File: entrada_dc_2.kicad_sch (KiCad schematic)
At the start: 4 parts

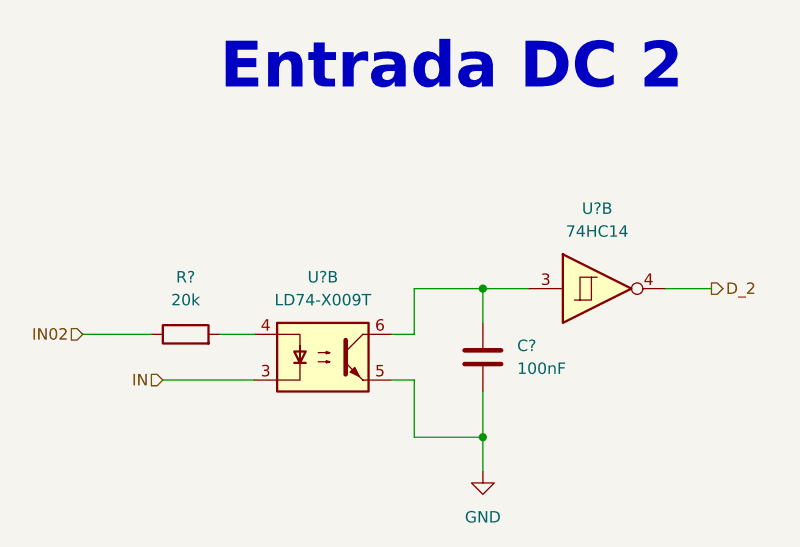
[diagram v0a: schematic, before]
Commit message: input/output separadas
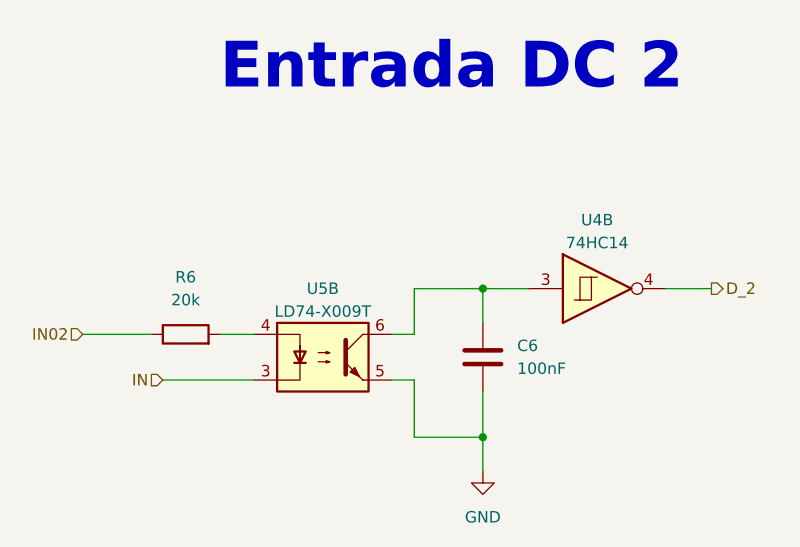
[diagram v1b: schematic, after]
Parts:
- gave numbers to parts that had none: 4
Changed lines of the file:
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@@
 (kicad_sch (version 20221004) (generator eeschema)
   (paper "A4" portrait)
+  (title_block
+    (date "2022-10-09")
+    (rev "José Luis Laica")
+  )
   (junction (at 113.03 138.43) (diameter 0) (color 0 0 0 0)
   )
@@
   (symbol (lib_id "power:GND") (at 113.03 142.24 0) (unit 1)
     (in_bom yes) (on_board yes) (dnp no) (fields_autoplaced)
-    (property "Reference" "#PWR?" (at 113.03 148.59 0)
+    (property "Reference" "#PWR07" (at 113.03 148.59 0)
       (effects (font (size 1.27 1.27)) hide)
     )
@@
       (project "PLC 32 V2"
         (path "/d17a54f1-6eda-453f-95e1-42a53b02a1c3/7b2fc48b-830b-4449-9557-444c529d204e"
-          (reference "#PWR?") (unit 1) (value "GND") (footprint "")
+          (reference "#PWR07") (unit 1) (value "GND") (footprint "")
         )
       )
@@
   (symbol (lib_id "Device:C") (at 113.03 129.54 0) (unit 1)
     (in_bom yes) (on_board yes) (dnp no) (fields_autoplaced)
-    (property "Reference" "C?" (at 116.84 128.2699 0)
+    (property "Reference" "C6" (at 116.84 128.2699 0)
       (effects (font (size 1.27 1.27)) (justify left))
     )
@@
       (project "PLC 32 V2"
         (path "/d17a54f1-6eda-453f-95e1-42a53b02a1c3/7b2fc48b-830b-4449-9557-444c529d204e"
-          (reference "C?") (unit 1) (value "100nF") (footprint "Capacitor_SMD:C_0402_1005Metric")
+          (reference "C6") (unit 1) (value "100nF") (footprint "Capacitor_SMD:C_0402_1005Metric")
         )
       )
@@
   (symbol (lib_id "Device:R") (at 80.01 127 90) (unit 1)
     (in_bom yes) (on_board yes) (dnp no) (fields_autoplaced)
-    (property "Reference" "R?" (at 80.01 120.65 90)
+    (property "Reference" "R6" (at 80.01 120.65 90)
       (effects (font (size 1.27 1.27)))
     )
@@
       (project "PLC 32 V2"
         (path "/d17a54f1-6eda-453f-95e1-42a53b02a1c3/7b2fc48b-830b-4449-9557-444c529d204e"
-          (reference "R?") (unit 1) (value "20k") (footprint "Resistor_SMD:R_0603_1608Metric")
+          (reference "R6") (unit 1) (value "20k") (footprint "Resistor_SMD:R_0603_1608Metric")
         )
       )
@@
   (symbol (lib_id "Isolator:ILD74") (at 95.25 129.54 0) (unit 2)
     (in_bom yes) (on_board yes) (dnp no) (fields_autoplaced)
-    (property "Reference" "U?" (at 95.25 120.65 0)
-      (effects (font (size 1.27 1.27)))
-    )
-    (property "Value" "LD74-X009T" (at 95.25 123.19 0)
+    (property "Reference" "U5" (at 95.25 121.92 0)
+      (effects (font (size 1.27 1.27)))
+    )
+    (property "Value" "LD74-X009T" (at 95.25 124.46 0)
       (effects (font (size 1.27 1.27)))
     )
@@
       (project "PLC 32 V2"
         (path "/d17a54f1-6eda-453f-95e1-42a53b02a1c3/7b2fc48b-830b-4449-9557-444c529d204e"
-          (reference "U?") (unit 2) (value "LD74-X009T") (footprint "Package_DIP:DIP-8_W8.89mm_SMDSocket_LongPads")
+          (reference "U5") (unit 2) (value "LD74-X009T") (footprint "Package_DIP:DIP-8_W8.89mm_SMDSocket_LongPads")
         )
       )
@@
   (symbol (lib_id "74xx:74HC14") (at 125.73 121.92 0) (unit 2)
     (in_bom yes) (on_board yes) (dnp no) (fields_autoplaced)
-    (property "Reference" "U?" (at 125.73 113.03 0)
-      (effects (font (size 1.27 1.27)))
-    )
-    (property "Value" "74HC14" (at 125.73 115.57 0)
+    (property "Reference" "U4" (at 125.73 114.3 0)
+      (effects (font (size 1.27 1.27)))
+    )
+    (property "Value" "74HC14" (at 125.73 116.84 0)
       (effects (font (size 1.27 1.27)))
     )
@@
       (project "PLC 32 V2"
         (path "/d17a54f1-6eda-453f-95e1-42a53b02a1c3/7b2fc48b-830b-4449-9557-444c529d204e"
-          (reference "U?") (unit 2) (value "74HC14") (footprint "Package_SO:SOIC-14W_7.5x9mm_P1.27mm")
-        )
-      )
+          (reference "U4") (unit 2) (value "74HC14") (footprint "Package_SO:SOIC-14W_7.5x9mm_P1.27mm")
+        )
+      )

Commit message: add
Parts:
- renumbered C6 to C7, R6 to R36, U4 to U7, U5 to U8
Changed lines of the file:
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@@
   (symbol (lib_id "Device:C") (at 113.03 129.54 0) (unit 1)
     (in_bom yes) (on_board yes) (dnp no) (fields_autoplaced)
-    (property "Reference" "C6" (at 116.84 128.2699 0)
+    (property "Reference" "C7" (at 116.84 128.2699 0)
       (effects (font (size 1.27 1.27)) (justify left))
     )
@@
       (project "PLC 32 V2"
         (path "/d17a54f1-6eda-453f-95e1-42a53b02a1c3/7b2fc48b-830b-4449-9557-444c529d204e"
-          (reference "C6") (unit 1) (value "100nF") (footprint "Capacitor_SMD:C_0402_1005Metric")
+          (reference "C7") (unit 1) (value "100nF") (footprint "Capacitor_SMD:C_0402_1005Metric")
         )
       )
@@
   (symbol (lib_id "Device:R") (at 80.01 127 90) (unit 1)
     (in_bom yes) (on_board yes) (dnp no) (fields_autoplaced)
-    (property "Reference" "R6" (at 80.01 120.65 90)
+    (property "Reference" "R36" (at 80.01 120.65 90)
       (effects (font (size 1.27 1.27)))
     )
@@
       (project "PLC 32 V2"
         (path "/d17a54f1-6eda-453f-95e1-42a53b02a1c3/7b2fc48b-830b-4449-9557-444c529d204e"
-          (reference "R6") (unit 1) (value "20k") (footprint "Resistor_SMD:R_0603_1608Metric")
+          (reference "R36") (unit 1) (value "20k") (footprint "Resistor_SMD:R_0603_1608Metric")
         )
       )
@@
   (symbol (lib_id "Isolator:ILD74") (at 95.25 129.54 0) (unit 2)
     (in_bom yes) (on_board yes) (dnp no) (fields_autoplaced)
-    (property "Reference" "U5" (at 95.25 121.92 0)
+    (property "Reference" "U8" (at 95.25 121.92 0)
       (effects (font (size 1.27 1.27)))
     )
@@
       (project "PLC 32 V2"
         (path "/d17a54f1-6eda-453f-95e1-42a53b02a1c3/7b2fc48b-830b-4449-9557-444c529d204e"
-          (reference "U5") (unit 2) (value "LD74-X009T") (footprint "Package_DIP:DIP-8_W8.89mm_SMDSocket_LongPads")
+          (reference "U8") (unit 2) (value "LD74-X009T") (footprint "Package_DIP:DIP-8_W8.89mm_SMDSocket_LongPads")
         )
       )
@@
   (symbol (lib_id "74xx:74HC14") (at 125.73 121.92 0) (unit 2)
     (in_bom yes) (on_board yes) (dnp no) (fields_autoplaced)
-    (property "Reference" "U4" (at 125.73 114.3 0)
+    (property "Reference" "U7" (at 125.73 114.3 0)
       (effects (font (size 1.27 1.27)))
     )
@@
       (project "PLC 32 V2"
         (path "/d17a54f1-6eda-453f-95e1-42a53b02a1c3/7b2fc48b-830b-4449-9557-444c529d204e"
-          (reference "U4") (unit 2) (value "74HC14") (footprint "Package_SO:SOIC-14W_7.5x9mm_P1.27mm")
+          (reference "U7") (unit 2) (value "74HC14") (footprint "Package_SO:SOIC-14W_7.5x9mm_P1.27mm")
         )
       )
